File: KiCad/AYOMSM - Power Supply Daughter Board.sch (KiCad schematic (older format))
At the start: 14 parts, among them J1 PWR_IN, J2 CONN_1, J3 CONN_2, J4 CONN_3, J5 CONN_4, J6 CONN_5

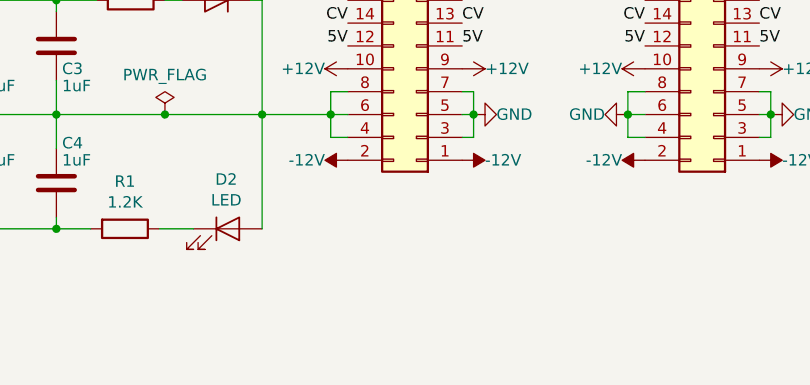
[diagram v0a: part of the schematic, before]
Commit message: Added 10-pin Power-In connector, updated layout
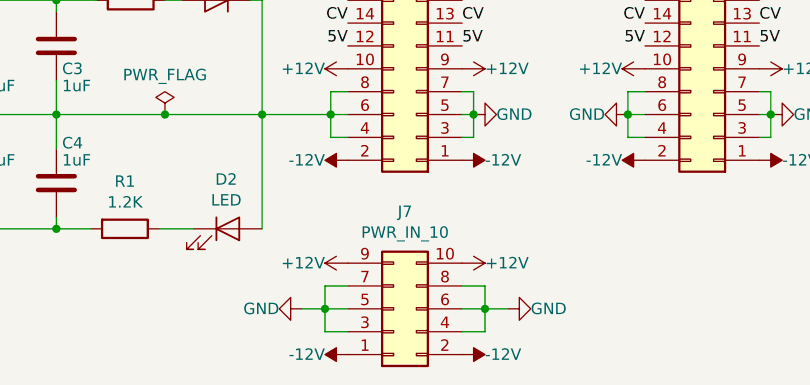
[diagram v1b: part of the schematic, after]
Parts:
- added J7: PWR_IN_10, Connector_IDC:IDC-Header_2x05_P2.54mm_Vertical, symbol Connector_Generic:Conn_02x05_Odd_Even
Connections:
- net +12V: now also J7.10 (Pin_10), J7.9 (Pin_9)
- net -12V: now also J7.1 (Pin_1), J7.2 (Pin_2)
- net GND: now also J7.3 (Pin_3), J7.4 (Pin_4), J7.5 (Pin_5), J7.6 (Pin_6), J7.7 (Pin_7), J7.8 (Pin_8)
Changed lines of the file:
@@
 Wire Wire Line
 	2350 3900 2775 3900
+$Comp
+L Connector_Generic:Conn_02x05_Odd_Even J7
+U 1 1 5F1647AA
+P 3350 4750
+F 0 "J7" H 3400 4325 50  0000 C CNN
+F 1 "PWR_IN_10" H 3400 4416 50  0000 C CNN
+F 2 "Connector_IDC:IDC-Header_2x05_P2.54mm_Vertical" H 3350 4750 50  0001 C CNN
+F 3 "~" H 3350 4750 50  0001 C CNN
+	1    3350 4750
+	1    0    0    1
+$EndComp
+$Comp
+L power:-12V #PWR03
+U 1 1 5F175890
+P 3150 4950
+F 0 "#PWR03" H 3150 5050 50  0001 C CNN
+F 1 "-12V" V 3150 5050 50  0000 L CNN
+F 2 "" H 3150 4950 50  0001 C CNN
+F 3 "" H 3150 4950 50  0001 C CNN
+	1    3150 4950
+	0    -1   -1   0
+$EndComp
+$Comp
+L power:-12V #PWR05
+U 1 1 5F175E16
+P 3650 4950
+F 0 "#PWR05" H 3650 5050 50  0001 C CNN
+F 1 "-12V" V 3650 5050 50  0000 L CNN
+F 2 "" H 3650 4950 50  0001 C CNN
+F 3 "" H 3650 4950 50  0001 C CNN
+	1    3650 4950
+	0    1    1    0
+$EndComp
+$Comp
+L power:+12V #PWR02
+U 1 1 5F17669C
+P 3150 4550
+F 0 "#PWR02" H 3150 4400 50  0001 C CNN
+F 1 "+12V" V 3150 4650 50  0000 L CNN
+F 2 "" H 3150 4550 50  0001 C CNN
+F 3 "" H 3150 4550 50  0001 C CNN
+	1    3150 4550
+	0    -1   -1   0
+$EndComp
+$Comp
+L power:+12V #PWR04
+U 1 1 5F176BFD
+P 3650 4550
+F 0 "#PWR04" H 3650 4400 50  0001 C CNN
+F 1 "+12V" V 3650 4650 50  0000 L CNN
+F 2 "" H 3650 4550 50  0001 C CNN
+F 3 "" H 3650 4550 50  0001 C CNN
+	1    3650 4550
+	0    1    1    0
+$EndComp
+$Comp
+L power:GND #PWR01
+U 1 1 5F1776C6
+P 2950 4750
+F 0 "#PWR01" H 2950 4500 50  0001 C CNN
+F 1 "GND" V 2950 4650 50  0000 R CNN
+F 2 "" H 2950 4750 50  0001 C CNN
+F 3 "" H 2950 4750 50  0001 C CNN
+	1    2950 4750
+	0    1    1    0
+$EndComp
+Wire Wire Line
+	3150 4850 3050 4850
+Wire Wire Line
+	3050 4850 3050 4750
+Wire Wire Line
+	3050 4650 3150 4650
+Wire Wire Line
+	3150 4750 3050 4750
+Connection ~ 3050 4750
+Wire Wire Line
+	3050 4750 3050 4650
+Wire Wire Line
+	2950 4750 3050 4750
+$Comp
+L power:GND #PWR06
+U 1 1 5F17F892
+P 3850 4750
+F 0 "#PWR06" H 3850 4500 50  0001 C CNN
+F 1 "GND" V 3850 4650 50  0000 R CNN
+F 2 "" H 3850 4750 50  0001 C CNN
+F 3 "" H 3850 4750 50  0001 C CNN
+	1    3850 4750
+	0    -1   -1   0
+$EndComp
+Wire Wire Line
+	3850 4750 3750 4750
+Wire Wire Line
+	3650 4650 3750 4650
+Wire Wire Line
+	3750 4650 3750 4750
+Connection ~ 3750 4750
+Wire Wire Line
+	3750 4750 3650 4750
+Wire Wire Line
+	3650 4850 3750 4850
+Wire Wire Line
+	3750 4850 3750 4750
 $EndSCHEMATC

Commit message: Updated BOM, ordering information, updated silkscreen, added README
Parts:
- C1, C2: Ordering (none) -> <a href=\"https://www.taydaelectronics.com/10uf-35v-105c-jr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
- C3, C4: Ordering (none) -> <a href=\"https://www.taydaelectronics.com/capacitors/monol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
- D1, D2: Ordering (none) -> <a href=\"https://www.taydaelectronics.com/leds/round-leds/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
- J1, J2, J3, J4, J5, J6, J7: Ordering (none) -> <a href=\"https://www.taydaelectronics.com/connectors-socke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
- R1, R2: Ordering (none) -> <a href=\"https://www.taydaelectronics.com/resistor-1-2k-oh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
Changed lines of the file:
@@
 encoding utf-8
 Sheet 1 1
-Title ""
-Date ""
-Rev ""
-Comp ""
+Title "Power Supply Bus"
+Date "2020-07-25"
+Rev "1.0"
+Comp "Shapetaker"
 Comment1 ""
 Comment2 ""
@@
 F 2 "Connector_IDC:IDC-Header_2x08_P2.54mm_Vertical" H 3450 3800 50  0001 C CNN
 F 3 "~" H 3450 3800 50  0001 C CNN
+F 4 "<a href=\"https://www.taydaelectronics.com/connectors-sockets/box-header-connectors/16-pin-box-header-connector-2-54mm.html\">Tayda</a>" H 3450 3800 50  0001 C CNN "Ordering"
 	1    3450 3800
 	-1   0    0    1
@@
 F 2 "Connector_IDC:IDC-Header_2x08_P2.54mm_Vertical" H 4750 3800 50  0001 C CNN
 F 3 "~" H 4750 3800 50  0001 C CNN
+F 4 "<a href=\"https://www.taydaelectronics.com/connectors-sockets/box-header-connectors/16-pin-box-header-connector-2-54mm.html\">Tayda</a>" H 4750 3800 50  0001 C CNN "Ordering"
 	1    4750 3800
 	-1   0    0    1
@@
 F 2 "Connector_IDC:IDC-Header_2x08_P2.54mm_Vertical" H 6025 3800 50  0001 C CNN
 F 3 "~" H 6025 3800 50  0001 C CNN
+F 4 "<a href=\"https://www.taydaelectronics.com/connectors-sockets/box-header-connectors/16-pin-box-header-connector-2-54mm.html\">Tayda</a>" H 6025 3800 50  0001 C CNN "Ordering"
 	1    6025 3800
 	-1   0    0    1
@@
 F 2 "Capacitor_THT:C_Radial_D6.3mm_H11.0mm_P2.50mm" H 1538 3450 50  0001 C CNN
 F 3 "~" H 1500 3600 50  0001 C CNN
+F 4 "<a href=\"https://www.taydaelectronics.com/10uf-35v-105c-jrb-radial-electrolytic-capacitor-5x11mm.html\">Tayda</a>" H 1500 3600 50  0001 C CNN "Ordering"
 	1    1500 3600
 	1    0    0    -1
@@
 F 2 "Capacitor_THT:C_Radial_D6.3mm_H11.0mm_P2.50mm" H 1538 4050 50  0001 C CNN
 F 3 "~" H 1500 4200 50  0001 C CNN
+F 4 "<a href=\"https://www.taydaelectronics.com/10uf-35v-105c-jrb-radial-electrolytic-capacitor-5x11mm.html\">Tayda</a>" H 1500 4200 50  0001 C CNN "Ordering"
 	1    1500 4200
 	1    0    0    -1
@@
 F 2 "Capacitor_THT:C_Disc_D4.7mm_W2.5mm_P5.00mm" H 1913 4050 50  0001 C CNN
 F 3 "~" H 1875 4200 50  0001 C CNN
+F 4 "<a href=\"https://www.taydaelectronics.com/capacitors/monolithic-ceramic-capacitor/1uf-50v-multilayer-ceramic-capacitor.html\">Tayda</a>" H 1875 4200 50  0001 C CNN "Ordering"
 	1    1875 4200
 	1    0    0    -1
@@
 F 2 "Connector_IDC:IDC-Header_2x08_P2.54mm_Vertical" H 7300 3800 50  0001 C CNN
 F 3 "~" H 7300 3800 50  0001 C CNN
+F 4 "<a href=\"https://www.taydaelectronics.com/connectors-sockets/box-header-connectors/16-pin-box-header-connector-2-54mm.html\">Tayda</a>" H 7300 3800 50  0001 C CNN "Ordering"
 	1    7300 3800
 	-1   0    0    1
@@
 F 2 "Connector_IDC:IDC-Header_2x08_P2.54mm_Vertical" H 8625 3800 50  0001 C CNN
 F 3 "~" H 8625 3800 50  0001 C CNN
+F 4 "<a href=\"https://www.taydaelectronics.com/connectors-sockets/box-header-connectors/16-pin-box-header-connector-2-54mm.html\">Tayda</a>" H 8625 3800 50  0001 C CNN "Ordering"
 	1    8625 3800
 	-1   0    0    1
@@
 F 2 "Connector_IDC:IDC-Header_2x08_P2.54mm_Vertical" H 9950 3800 50  0001 C CNN
 F 3 "~" H 9950 3800 50  0001 C CNN
+F 4 "<a href=\"https://www.taydaelectronics.com/connectors-sockets/box-header-connectors/16-pin-box-header-connector-2-54mm.html\">Tayda</a>" H 9950 3800 50  0001 C CNN "Ordering"
 	1    9950 3800
 	-1   0    0    1
@@
 F 2 "Capacitor_THT:C_Disc_D4.7mm_W2.5mm_P5.00mm" H 1913 3450 50  0001 C CNN
 F 3 "~" H 1875 3600 50  0001 C CNN
+F 4 "<a href=\"https://www.taydaelectronics.com/capacitors/monolithic-ceramic-capacitor/1uf-50v-multilayer-ceramic-capacitor.html\">Tayda</a>" H 1875 3600 50  0001 C CNN "Ordering"
 	1    1875 3600
 	1    0    0    -1
@@
 F 2 "Resistor_THT:R_Axial_DIN0207_L6.3mm_D2.5mm_P7.62mm_Horizontal" V 2130 3400 50  0001 C CNN
 F 3 "~" H 2200 3400 50  0001 C CNN
+F 4 "<a href=\"https://www.taydaelectronics.com/resistor-1-2k-ohm-1-4w-1-metal-film-pkg-of-10.html\">Tayda</a>" V 2200 3400 50  0001 C CNN "Ordering"
 	1    2200 3400
 	0    1    1    0
@@
 F 2 "Resistor_THT:R_Axial_DIN0207_L6.3mm_D2.5mm_P7.62mm_Horizontal" V 2105 4400 50  0001 C CNN
 F 3 "~" H 2175 4400 50  0001 C CNN
+F 4 "<a href=\"https://www.taydaelectronics.com/resistor-1-2k-ohm-1-4w-1-metal-film-pkg-of-10.html\">Tayda</a>" V 2175 4400 50  0001 C CNN "Ordering"
 	1    2175 4400
 	0    1    1    0
@@
 F 2 "LED_THT:LED_D3.0mm" H 2625 4400 50  0001 C CNN
 F 3 "~" H 2625 4400 50  0001 C CNN
+F 4 "<a href=\"https://www.taydaelectronics.com/leds/round-leds/3mm-leds/blue/led-3mm-blue-diffuse-lens.html\">Tayda</a>" H 2625 4400 50  0001 C CNN "Ordering"
 	1    2625 4400
 	1    0    0    -1
@@
 F 2 "LED_THT:LED_D3.0mm" H 2575 3400 50  0001 C CNN
 F 3 "~" H 2575 3400 50  0001 C CNN
+F 4 "<a href=\"https://www.taydaelectronics.com/leds/round-leds/3mm-leds/led-3mm-orange.html\">Tayda</a>" H 2575 3400 50  0001 C CNN "Ordering"
 	1    2575 3400
 	-1   0    0    1
@@
 F 2 "Connector_IDC:IDC-Header_2x05_P2.54mm_Vertical" H 3350 4750 50  0001 C CNN
 F 3 "~" H 3350 4750 50  0001 C CNN
+F 4 "<a href=\"https://www.taydaelectronics.com/connectors-sockets/box-header-connectors/10-pin-box-header-connector-2-54mm.html\">Tayda</a>" H 3350 4750 50  0001 C CNN "Ordering"
 	1    3350 4750
 	1    0    0    1
